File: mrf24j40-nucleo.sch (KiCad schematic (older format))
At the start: 2 parts, among them M1 MRF24J40MA_TRANSEIVER_MODULE, P1 CONN_02X08

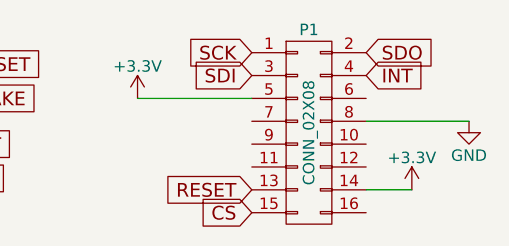
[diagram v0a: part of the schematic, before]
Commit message: Fix in 3.3V pin/Minor reroute
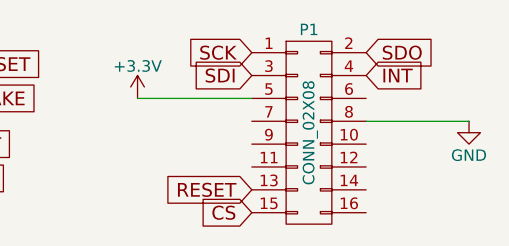
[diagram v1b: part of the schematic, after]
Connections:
- net +3V3: no longer P1.14 (P14)
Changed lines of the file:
@@
 Title ""
 Date "2017-01-22"
-Rev ""
+Rev "1.1"
 Comp ""
 Comment1 ""
@@
 	5500 1250 5950 1250
 $Comp
-L +3.3V #PWR05
-U 1 1 5884BC0A
-P 5700 1550
-F 0 "#PWR05" H 5700 1400 50  0001 C CNN
-F 1 "+3.3V" H 5700 1690 50  0000 C CNN
-F 2 "" H 5700 1550 60  0000 C CNN
-F 3 "" H 5700 1550 60  0000 C CNN
-	1    5700 1550
-	1    0    0    -1
-$EndComp
-Wire Wire Line
-	5700 1550 5500 1550
-$Comp
 L CONN_02X08 P1
